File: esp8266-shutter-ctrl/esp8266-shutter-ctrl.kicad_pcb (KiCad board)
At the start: 2 copper layers, 0 parts

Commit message: shutter-ctrl: pcb: first try
Signed-off-by: Dominik Laton <dominik.laton@web.de>
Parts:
- added C1: 100n, Capacitor_SMD:C_0805_2012Metric_Pad1.18x1.45mm_HandSolder, B.Cu at (104.1, 94.4)
- added C10: 100n, Capacitor_SMD:C_0805_2012Metric_Pad1.18x1.45mm_HandSolder, B.Cu at (124.8, 120.2)
- added C11: 100n, Capacitor_SMD:C_0805_2012Metric_Pad1.18x1.45mm_HandSolder, B.Cu at (145.4, 120.1)
- added C12: 100n, Capacitor_SMD:C_0805_2012Metric_Pad1.18x1.45mm_HandSolder, B.Cu at (165.9, 120.1)
- added C13: 100n, Capacitor_SMD:C_0805_2012Metric_Pad1.18x1.45mm_HandSolder, B.Cu at (186.9, 120.0)
- added C14: 100n, Capacitor_SMD:C_0805_2012Metric_Pad1.18x1.45mm_HandSolder, B.Cu at (207.1, 120.0)
- added C15: 100n, Capacitor_SMD:C_0805_2012Metric_Pad1.18x1.45mm_HandSolder, B.Cu at (227.7, 129.1)
- added C16: 100n, Capacitor_SMD:C_0805_2012Metric_Pad1.18x1.45mm_HandSolder, B.Cu at (248.3, 120.0)
- added C17: 4.7uF, Capacitor_SMD:C_0805_2012Metric_Pad1.18x1.45mm_HandSolder, B.Cu at (115.5, 140.1)
- added C18: 2.2uF, Capacitor_SMD:C_0805_2012Metric_Pad1.18x1.45mm_HandSolder, B.Cu at (131.4, 139.8)
- added C2: 100n, Capacitor_SMD:C_0805_2012Metric_Pad1.18x1.45mm_HandSolder, B.Cu at (124.7, 94.4)
- added C3: 100n, Capacitor_SMD:C_0805_2012Metric_Pad1.18x1.45mm_HandSolder, B.Cu at (145.4, 94.4)
- added C4: 100n, Capacitor_SMD:C_0805_2012Metric_Pad1.18x1.45mm_HandSolder, B.Cu at (165.3, 94.5)
- added C5: 100n, Capacitor_SMD:C_0805_2012Metric_Pad1.18x1.45mm_HandSolder, B.Cu at (189.4, 90.9)
- added C6: 100n, Capacitor_SMD:C_0805_2012Metric_Pad1.18x1.45mm_HandSolder, B.Cu at (207.1, 94.4)
- added C7: 100n, Capacitor_SMD:C_0805_2012Metric_Pad1.18x1.45mm_HandSolder, B.Cu at (227.6, 94.5)
- added C8: 100n, Capacitor_SMD:C_0805_2012Metric_Pad1.18x1.45mm_HandSolder, B.Cu at (248.3, 94.4)
- added C9: 100n, Capacitor_SMD:C_0805_2012Metric_Pad1.18x1.45mm_HandSolder, B.Cu at (104.2, 120.1)
- added H1: MountingHole, MountingHole:MountingHole_4.3mm_M4_ISO14580_Pad, F.Cu at (95.8, 75.8)
- added H2: MountingHole, MountingHole:MountingHole_4.3mm_M4_ISO14580_Pad, F.Cu at (264.2, 75.8)
- added H3: MountingHole, MountingHole:MountingHole_4.3mm_M4_ISO14580_Pad, F.Cu at (264.2, 144.2)
- added H4: MountingHole, MountingHole:MountingHole_4.3mm_M4_ISO14580_Pad, F.Cu at (95.8, 144.2)
- added J1: Conn_01x08_Male, Connector_Wago:Wago_734-138_1x08_P3.50mm_Vertical, B.Cu at (223.1, 143.1)
- added J2: Conn_01x08_Male, Connector_Wago:Wago_734-138_1x08_P3.50mm_Vertical, B.Cu at (255.8, 143.1)
- added J3: Conn_01x04_Male, Connector_Wago:Wago_734-134_1x04_P3.50mm_Vertical, B.Cu at (170.1, 143.1)
- added J4: Conn_01x02_Male, Connector_Wago:Wago_734-132_1x02_P3.50mm_Vertical, B.Cu at (108.7, 141.2)
- added J5: Conn_01x04_Male, Connector_JST:JST_XH_B4B-XH-A_1x04_P2.50mm_Vertical, B.Cu at (221.6, 101.3)
- added J6: Conn_01x02_Male, Connector_JST:JST_XH_B2B-XH-A_1x02_P2.50mm_Vertical, B.Cu at (149.0, 143.1)
- added J7: Conn_01x04_Male, Connector_JST:JST_XH_B4B-XH-A_1x04_P2.50mm_Vertical, B.Cu at (159.2, 121.6)
- added L1: 4.7uH, Inductor_THT:L_Radial_D8.7mm_P5.00mm_Fastron_07HCP, B.Cu at (121.4, 140.9)
- added R1: 33k, Resistor_SMD:R_0805_2012Metric_Pad1.20x1.40mm_HandSolder, F.Cu at (104.1, 87.1)
- added R10: 16, Resistor_SMD:R_0805_2012Metric_Pad1.20x1.40mm_HandSolder, F.Cu at (132.3, 87.1)
- added R11: 16, Resistor_SMD:R_0805_2012Metric_Pad1.20x1.40mm_HandSolder, F.Cu at (153.0, 87.3)
- added R12: 16, Resistor_SMD:R_0805_2012Metric_Pad1.20x1.40mm_HandSolder, F.Cu at (176.7, 91.0)
- added R13: 16, Resistor_SMD:R_0805_2012Metric_Pad1.20x1.40mm_HandSolder, F.Cu at (194.1, 87.2)
- added R14: 16, Resistor_SMD:R_0805_2012Metric_Pad1.20x1.40mm_HandSolder, F.Cu at (214.8, 87.3)
- added R15: 16, Resistor_SMD:R_0805_2012Metric_Pad1.20x1.40mm_HandSolder, F.Cu at (235.3, 87.3)
- added R16: 16, Resistor_SMD:R_0805_2012Metric_Pad1.20x1.40mm_HandSolder, F.Cu at (255.9, 87.3)
- added R17: 33k, Resistor_SMD:R_0805_2012Metric_Pad1.20x1.40mm_HandSolder, F.Cu at (104.1, 112.6)
- added R18: 33k, Resistor_SMD:R_0805_2012Metric_Pad1.20x1.40mm_HandSolder, F.Cu at (124.6, 112.9)
- added R19: 33k, Resistor_SMD:R_0805_2012Metric_Pad1.20x1.40mm_HandSolder, F.Cu at (145.3, 112.7)
- added R2: 33k, Resistor_SMD:R_0805_2012Metric_Pad1.20x1.40mm_HandSolder, F.Cu at (124.7, 87.1)
- added R20: 33k, Resistor_SMD:R_0805_2012Metric_Pad1.20x1.40mm_HandSolder, F.Cu at (165.9, 112.6)
- added R21: 33k, Resistor_SMD:R_0805_2012Metric_Pad1.20x1.40mm_HandSolder, F.Cu at (186.5, 112.8)
- added R22: 33k, Resistor_SMD:R_0805_2012Metric_Pad1.20x1.40mm_HandSolder, F.Cu at (202.9, 116.6)
- added R23: 33k, Resistor_SMD:R_0805_2012Metric_Pad1.20x1.40mm_HandSolder, F.Cu at (227.6, 112.8)
- added R24: 33k, Resistor_SMD:R_0805_2012Metric_Pad1.20x1.40mm_HandSolder, F.Cu at (248.3, 112.6)
- added R25: 16, Resistor_SMD:R_0805_2012Metric_Pad1.20x1.40mm_HandSolder, F.Cu at (111.8, 112.7)
- added R26: 16, Resistor_SMD:R_0805_2012Metric_Pad1.20x1.40mm_HandSolder, F.Cu at (132.3, 112.9)
- added R27: 16, Resistor_SMD:R_0805_2012Metric_Pad1.20x1.40mm_HandSolder, F.Cu at (152.9, 112.8)
- added R28: 16, Resistor_SMD:R_0805_2012Metric_Pad1.20x1.40mm_HandSolder, F.Cu at (173.5, 113.0)
- added R29: 16, Resistor_SMD:R_0805_2012Metric_Pad1.20x1.40mm_HandSolder, F.Cu at (194.1, 112.9)
- added R3: 33k, Resistor_SMD:R_0805_2012Metric_Pad1.20x1.40mm_HandSolder, F.Cu at (145.2, 87.3)
- added R30: 16, Resistor_SMD:R_0805_2012Metric_Pad1.20x1.40mm_HandSolder, F.Cu at (215.7, 113.8)
- added R31: 16, Resistor_SMD:R_0805_2012Metric_Pad1.20x1.40mm_HandSolder, F.Cu at (235.3, 112.8)
- added R32: 16, Resistor_SMD:R_0805_2012Metric_Pad1.20x1.40mm_HandSolder, F.Cu at (256.0, 112.8)
- added R33: 10k, Resistor_SMD:R_0805_2012Metric_Pad1.20x1.40mm_HandSolder, F.Cu at (168.1, 112.7)
- added R34: 10k, Resistor_SMD:R_0805_2012Metric_Pad1.20x1.40mm_HandSolder, F.Cu at (163.5, 112.7)
- added R35: 10k, Resistor_SMD:R_0805_2012Metric_Pad1.20x1.40mm_HandSolder, F.Cu at (161.4, 112.8)
- added R36: 10k, Resistor_SMD:R_0805_2012Metric_Pad1.20x1.40mm_HandSolder, F.Cu at (191.6, 112.8)
- added R37: 10k, Resistor_SMD:R_0805_2012Metric_Pad1.20x1.40mm_HandSolder, F.Cu at (189.4, 112.8)
- added R38: 10k, Resistor_SMD:R_0805_2012Metric_Pad1.20x1.40mm_HandSolder, B.Cu at (190.6, 120.0)
- added R39: 10k, Resistor_SMD:R_0805_2012Metric_Pad1.20x1.40mm_HandSolder, F.Cu at (234.3, 108.0)
- added R4: 33k, Resistor_SMD:R_0805_2012Metric_Pad1.20x1.40mm_HandSolder, F.Cu at (165.2, 87.4)
- added R40: 10k, Resistor_SMD:R_0805_2012Metric_Pad1.20x1.40mm_HandSolder, F.Cu at (231.0, 110.9)
- added R41: 10k, Resistor_SMD:R_0805_2012Metric_Pad1.20x1.40mm_HandSolder, B.Cu at (236.2, 109.6)
- added R5: 33k, Resistor_SMD:R_0805_2012Metric_Pad1.20x1.40mm_HandSolder, F.Cu at (182.7, 90.9)
- added R6: 33k, Resistor_SMD:R_0805_2012Metric_Pad1.20x1.40mm_HandSolder, F.Cu at (207.0, 87.3)
- added R7: 33k, Resistor_SMD:R_0805_2012Metric_Pad1.20x1.40mm_HandSolder, F.Cu at (227.7, 87.3)
- added R8: 33k, Resistor_SMD:R_0805_2012Metric_Pad1.20x1.40mm_HandSolder, F.Cu at (248.3, 87.2)
- added R9: 16, Resistor_SMD:R_0805_2012Metric_Pad1.20x1.40mm_HandSolder, F.Cu at (111.8, 87.2)
- added RN1: 3k3, Resistor_THT:R_Array_SIP9, B.Cu at (197.7, 106.9)
- added RN2: 3k3, Resistor_THT:R_Array_SIP9, B.Cu at (182.0, 132.8)
- added RN3: 10k, Resistor_THT:R_Array_SIP9, B.Cu at (218.1, 110.9)
- added RN4: 10k, Resistor_THT:R_Array_SIP9, B.Cu at (167.3, 86.1)
- added RN5: 10k, Resistor_THT:R_Array_SIP9, B.Cu at (239.0, 103.4)
- added RN6: 10k, Resistor_THT:R_Array_SIP9, B.Cu at (221.0, 135.1)
- added SW1: SW_MEC_5G_LED, Button_Switch_SMD:SW_MEC_5GSH9, F.Cu at (107.9, 97.2)
- added SW10: SW_MEC_5G_LED, Button_Switch_SMD:SW_MEC_5GSH9, F.Cu at (128.5, 122.8)
- added SW11: SW_MEC_5G_LED, Button_Switch_SMD:SW_MEC_5GSH9, F.Cu at (149.1, 122.8)
- added SW12: SW_MEC_5G_LED, Button_Switch_SMD:SW_MEC_5GSH9, F.Cu at (169.7, 122.8)
- added SW13: SW_MEC_5G_LED, Button_Switch_SMD:SW_MEC_5GSH9, F.Cu at (190.3, 122.8)
- added SW14: SW_MEC_5G_LED, Button_Switch_SMD:SW_MEC_5GSH9, F.Cu at (210.9, 122.8)
- added SW15: SW_MEC_5G_LED, Button_Switch_SMD:SW_MEC_5GSH9, F.Cu at (231.5, 122.8)
- added SW16: SW_MEC_5G_LED, Button_Switch_SMD:SW_MEC_5GSH9, F.Cu at (252.1, 122.8)
- added SW2: SW_MEC_5G_LED, Button_Switch_SMD:SW_MEC_5GSH9, F.Cu at (128.5, 97.2)
- added SW3: SW_MEC_5G_LED, Button_Switch_SMD:SW_MEC_5GSH9, F.Cu at (149.1, 97.2)
- added SW4: SW_MEC_5G_LED, Button_Switch_SMD:SW_MEC_5GSH9, F.Cu at (169.1, 97.2)
- added SW5: SW_MEC_5G_LED, Button_Switch_SMD:SW_MEC_5GSH9, F.Cu at (190.3, 97.2)
- added SW6: SW_MEC_5G_LED, Button_Switch_SMD:SW_MEC_5GSH9, F.Cu at (210.9, 97.2)
- added SW7: SW_MEC_5G_LED, Button_Switch_SMD:SW_MEC_5GSH9, F.Cu at (231.5, 97.2)
- added SW8: SW_MEC_5G_LED, Button_Switch_SMD:SW_MEC_5GSH9, F.Cu at (252.1, 97.2)
- added SW9: SW_MEC_5G_LED, Button_Switch_SMD:SW_MEC_5GSH9, F.Cu at (107.9, 122.8)
- added U1: MCP23017_SO, Package_SO:SOIC-28W_7.5x17.9mm_P1.27mm, B.Cu at (159.9, 111.9)
- added U2: MCP23017_SO, Package_SO:SOIC-28W_7.5x17.9mm_P1.27mm, B.Cu at (182.8, 111.2)
- added U3: ULN2803A, Package_SO:SOIC-18W_7.5x11.6mm_P1.27mm, B.Cu at (179.6, 98.7)
- added U4: ULN2803A, Package_SO:SOIC-18W_7.5x11.6mm_P1.27mm, B.Cu at (179.6, 123.7)
- added U5: MCP23017_SO, Package_SO:SOIC-28W_7.5x17.9mm_P1.27mm, B.Cu at (229.0, 117.7)
- added U6: ULN2803A, Package_SO:SOIC-18W_7.5x11.6mm_P1.27mm, B.Cu at (212.6, 131.9)
- added U7: ULN2803A, Package_SO:SOIC-18W_7.5x11.6mm_P1.27mm, B.Cu at (245.3, 131.9)
- added U8: TEC2-1211WI, Converter_DCDC:Converter_DCDC_TRACO_TMR-xxxx_THT, B.Cu at (140.2, 142.4)
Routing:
- net /buttons/shutter_7_up_sw: track 0.00 -> 108.6 mm, vias 0 -> 2
- net /buttons/shutter_7_dn_sw: track 0.00 -> 106.4 mm, vias 0 -> 2
- net /buttons/shutter_6_dn_sw: track 0.00 -> 92.7 mm, vias 0 -> 2
- net /connectors/+12V_SWITCHED: track 0.00 -> 91.8 mm
- net Net-(RN1-Pad2): track 0.00 -> 90.3 mm
- net /buttons/shutter_6_up_sw: track 0.00 -> 87.7 mm, vias 0 -> 2
- net /buttons/shutter_0_dn_led: track 0.00 -> 83.4 mm, vias 0 -> 1
- net /buttons/shutter_0_up_led: track 0.00 -> 79.4 mm, vias 0 -> 1
- net /buttons/shutter_7_dn_led: track 0.00 -> 78.0 mm, vias 0 -> 1
- net Net-(RN2-Pad2): track 0.00 -> 75.5 mm
- net SDA: track 0.00 -> 74.6 mm, vias 0 -> 2
- net /buttons/shutter_7_up_led: track 0.00 -> 73.8 mm, vias 0 -> 1
- net Net-(RN1-Pad3): track 0.00 -> 72.3 mm
- net SCL: track 0.00 -> 71.9 mm, vias 0 -> 2
- net /buttons/shutter_0_dn_sw: track 0.00 -> 66.9 mm, vias 0 -> 2
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- added copper zone on F.Cu, net +3V3
- added copper zone on B.Cu, net GND
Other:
- board outline added: 180 x 80 mm

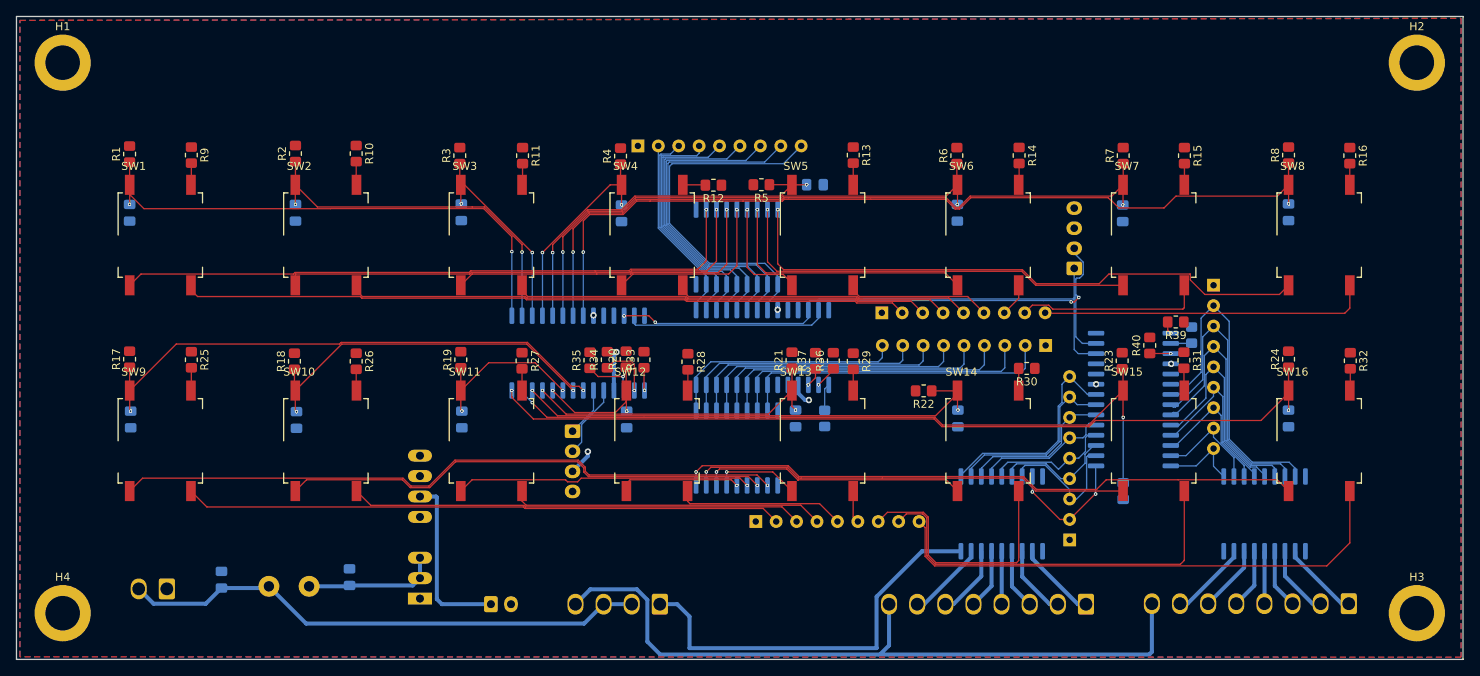
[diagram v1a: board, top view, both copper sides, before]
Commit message: shutter-ctrl: added fuse and increased track width for +12V
Signed-off-by: Dominik Laton <dominik.laton@web.de>
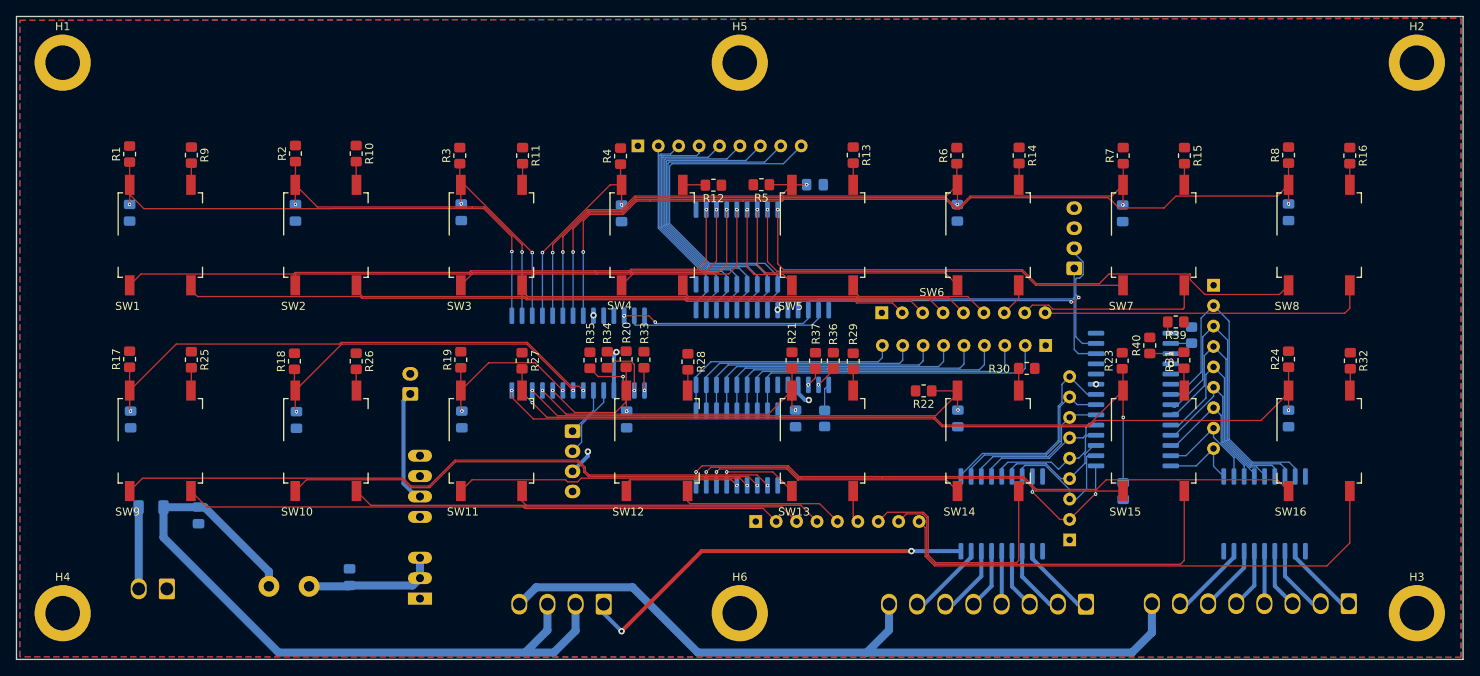
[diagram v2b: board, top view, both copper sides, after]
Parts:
- added F1: 13.2V/0.5A, Resistor_SMD:R_1206_3216Metric_Pad1.30x1.75mm_HandSolder, B.Cu at (106.7, 131.1)
- added H5: MountingHole, MountingHole:MountingHole_4.3mm_M4_ISO14580_Pad, F.Cu at (180.0, 75.8)
- added H6: MountingHole, MountingHole:MountingHole_4.3mm_M4_ISO14580_Pad, F.Cu at (180.0, 144.2)
- moved J6 28.0 mm to (139.0, 117.0), turned to 90 degrees
- moved C17 8.50 mm to (112.6, 132.1), turned to 270 degrees
- moved J3 6.98 mm to (163.1, 143.1)
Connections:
- J4 pad 2: +12V -> Net-(F1-Pad1)
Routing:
- net +12V: track 65.9 -> 90.9 mm
- net Net-(F1-Pad1): track 0.00 -> 10.2 mm
- net +5V: track 21.8 -> 14.2 mm
- net /connectors/+12V_SWITCHED: track 91.8 -> 94.8 mm
- net /connectors/shutter_en_+12V: track 50.8 -> 50.6 mm, vias 0 -> 2
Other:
- net class Super added: clearance 0.5, trace_width 1, via_dia 0.8, via_drill 0.4

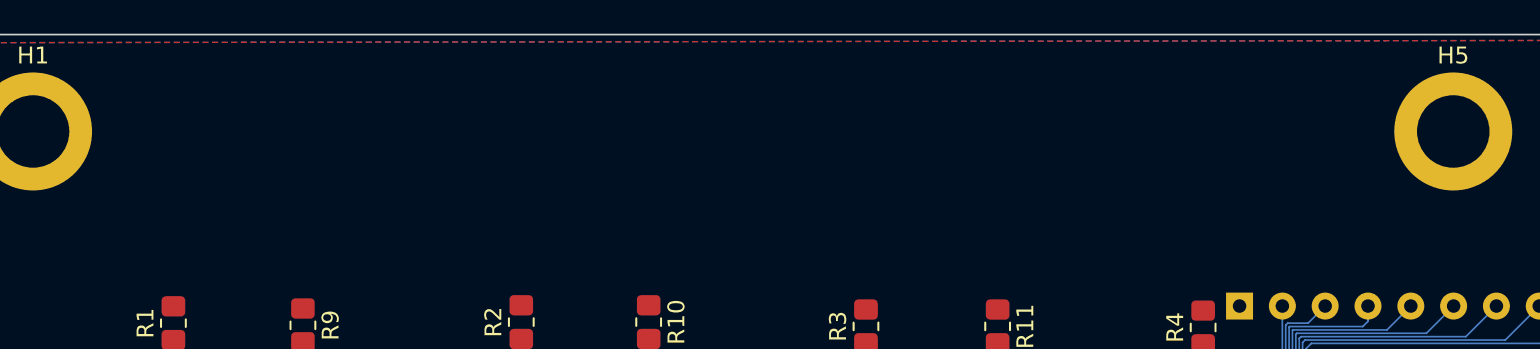
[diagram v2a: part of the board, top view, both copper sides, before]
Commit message: shutter-ctrl: pcb: added description
Signed-off-by: Dominik Laton <dominik.laton@web.de>
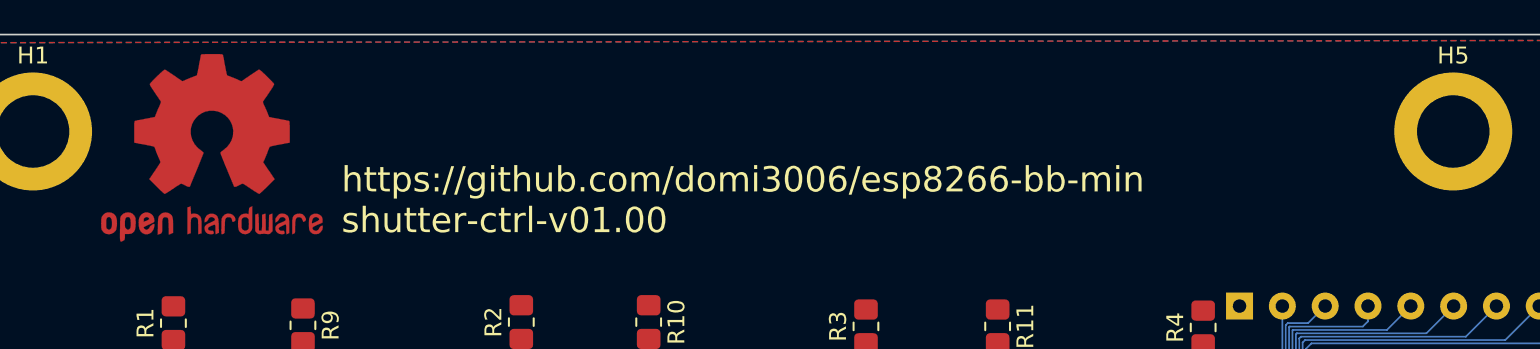
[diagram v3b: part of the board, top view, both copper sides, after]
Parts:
- added REF**: OSHW-Logo2_14.6x12mm_Copper, Symbol:OSHW-Logo2_14.6x12mm_Copper, F.Cu at (106.4, 76.7)
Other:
- board text added: "1: +12V_EN 2: +12V 3: +12V 4: +12V_SWITCHED"
- board text added: "1: +5V 2: GND"
- board text added: "1: 0_down 2: 1_down 3: 2_down 4: 3_down 5: 4_down 6: 5_down 7: 6_down 8: +12V_SWITCHED"
- board text added: "1: 0_up 2: 1_up 3: 2_up 4: 3_up 5: 4_up 6: 5_up 7: 6_up 8: +12V_SWITCHED"
- board text added: "1: GND 2: +12V"
- board text added: "1: INT_B 2: INT_A 3: +3V3 4: GND"
- board text added: "1: SCL 2: SDA 3: +3V3 4: GND"
- board text added: "https://github.com/domi3006/esp8266-bb-min shutter-ctrl-v01.00"

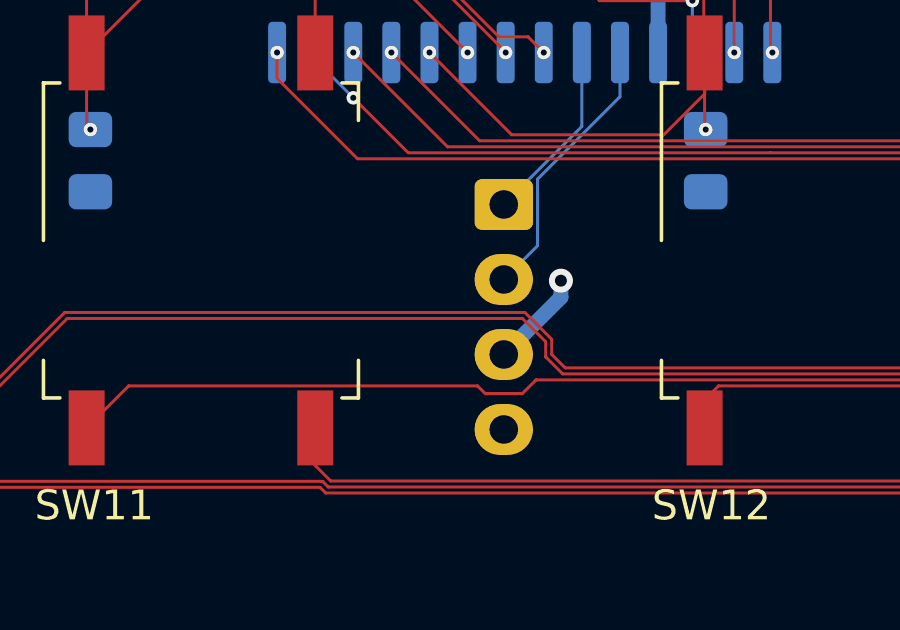
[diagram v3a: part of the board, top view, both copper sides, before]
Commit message: shutter-ctrl: pcb: improved 3V3 plane connection to J7
Signed-off-by: Dominik Laton <dominik.laton@web.de>
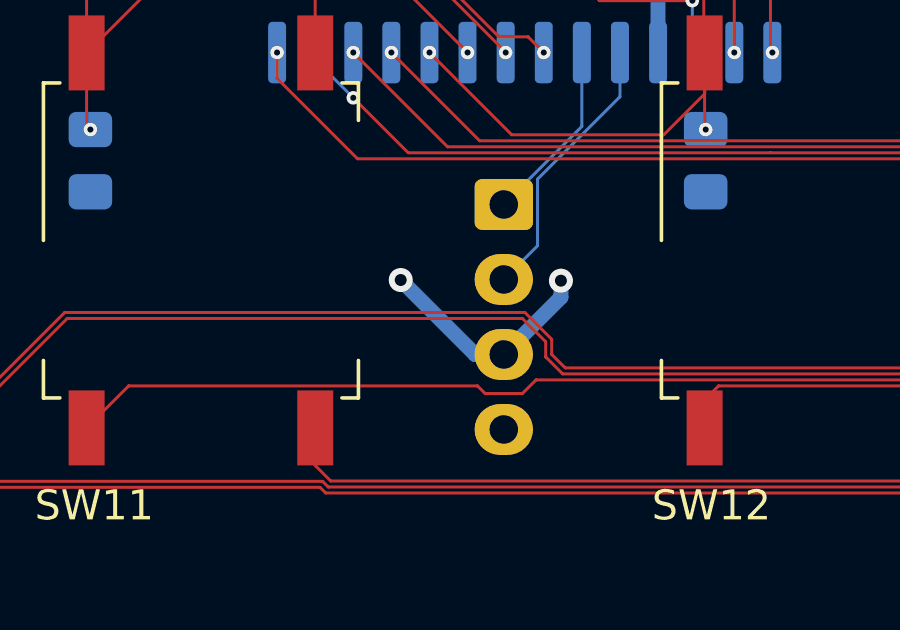
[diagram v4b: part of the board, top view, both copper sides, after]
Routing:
- net +3V3: track 10.9 -> 15.3 mm, vias 7 -> 8
